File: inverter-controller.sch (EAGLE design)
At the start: 168 parts, among them IC1 STM32F334C8T6, IC10 ISO3082, IC2 SY7152ABC, IC3 LMV358MMX, IC4 LMV358MMX, IC5 SY7152ABC, J1 621006245821, J2 61300211121, J3 CONNECTOR-SMD-2PIN, J4 CONNECTOR-SMD-2PIN, J5 CONNECTOR-SMD-2PIN, X3 0289-9068**15EDGVC-3.81-03P-14, X6 1365-16, Y1 NX2016SA-32M

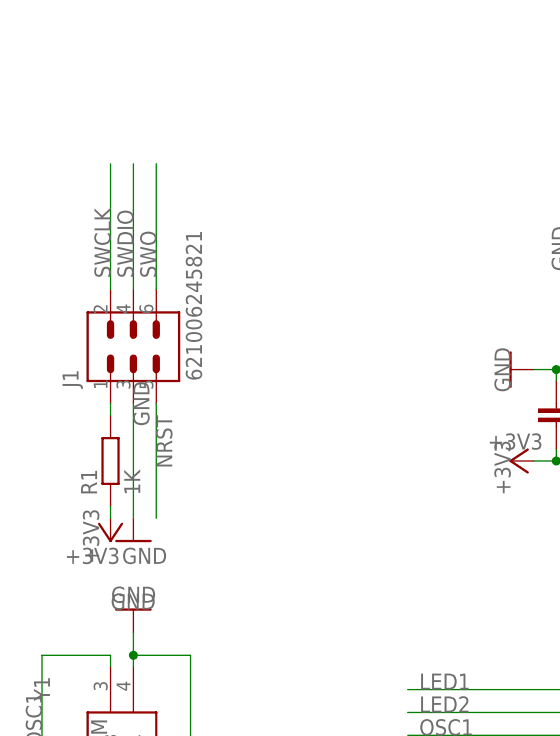
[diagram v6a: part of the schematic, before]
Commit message: Programlama soketi degistirildi.
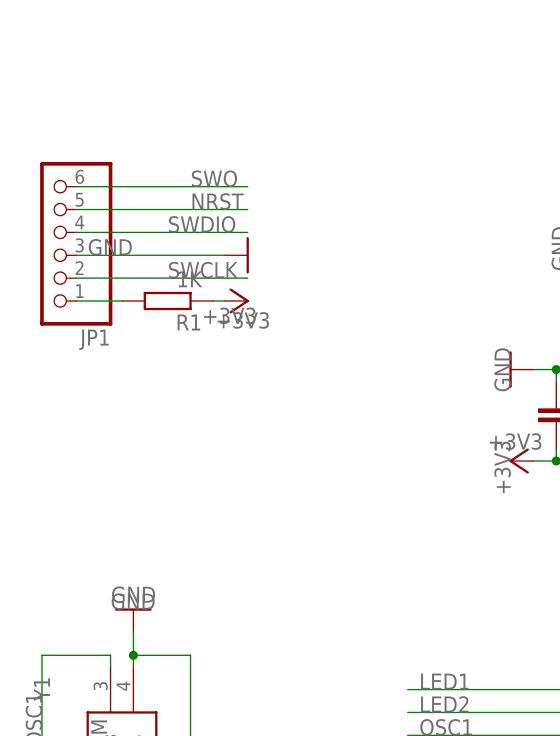
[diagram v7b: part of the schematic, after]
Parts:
- removed J1: 621006245821, Headers:621006245821
- added JP1: (no value), adafruit:PINHD-1X6
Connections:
- removed net N$11: J1.1, R1.2
- new net N$30: JP1.1, R1.2
- net GND: now also JP1.3; no longer J1.3
- net NRST: now also JP1.5; no longer J1.5
- net SWCLK: now also JP1.2; no longer J1.2
- net SWDIO: now also JP1.4; no longer J1.4
- net SWO: now also JP1.6; no longer J1.6
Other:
- moved on the sheet: R1
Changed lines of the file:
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@@
 <part name="TP2" library="testpad" library_urn="urn:adsk.eagle:library:385" deviceset="TP" device="B1,27" package3d_urn="urn:adsk.eagle:package:27944/2"/>
 <part name="TP3" library="testpad" library_urn="urn:adsk.eagle:library:385" deviceset="TP" device="B1,27" package3d_urn="urn:adsk.eagle:package:27944/2"/>
-<part name="J1" library="Headers" library_urn="urn:adsk.eagle:library:11687645" deviceset="621006245821" device="" package3d_urn="urn:adsk.eagle:package:11431832/2"/>
 <part name="+3V1" library="supply1" library_urn="urn:adsk.eagle:library:371" deviceset="+3V3" device=""/>
 <part name="Y1" library="enko" library_urn="urn:adsk.eagle:library:26809666" deviceset="NX2016SA-32M" device="" package3d_urn="urn:adsk.eagle:package:26812247/2"/>
-<part name="GND1" library="supply1" library_urn="urn:adsk.eagle:library:371" deviceset="GND" device=""/>
 <part name="J2" library="Headers" library_urn="urn:adsk.eagle:library:11687645" deviceset="61300211121" device="" package3d_urn="urn:adsk.eagle:package:11390690/2"/>
 <part name="+3V2" library="supply1" library_urn="urn:adsk.eagle:library:371" deviceset="+3V3" device=""/>
@@
 <part name="H3" library="holes" library_urn="urn:adsk.eagle:library:237" deviceset="MOUNT-PAD-ROUND" device="2.8" package3d_urn="urn:adsk.eagle:package:14281/1"/>
 <part name="H4" library="holes" library_urn="urn:adsk.eagle:library:237" deviceset="MOUNT-PAD-ROUND" device="2.8" package3d_urn="urn:adsk.eagle:package:14281/1"/>
+<part name="JP1" library="adafruit" library_urn="urn:adsk.eagle:library:420" deviceset="PINHD-1X6" device="" package3d_urn="urn:adsk.eagle:package:6240711/1"/>
+<part name="GND40" library="supply1" library_urn="urn:adsk.eagle:library:371" deviceset="GND" device=""/>
 </parts>
 <sheets>
@@
 <attribute name="TP_SIGNAL_NAME" x="81.28" y="26.67" size="1.778" layer="97" rot="R180"/>
 </instance>
-<instance part="J1" gate="G$1" x="19.05" y="113.03" smashed="yes" rot="R90">
-<attribute name="NAME" x="12.954" y="109.728" size="1.778" layer="95" rot="R90"/>
-<attribute name="VALUE" x="26.67" y="110.49" size="1.778" layer="96" rot="R90"/>
-</instance>
-<instance part="+3V1" gate="G$1" x="16.51" y="92.71" smashed="yes" rot="R180">
-<attribute name="VALUE" x="15.24" y="90.17" size="1.778" layer="96" rot="R90"/>
+<instance part="+3V1" gate="G$1" x="31.75" y="119.38" smashed="yes" rot="R270">
+<attribute name="VALUE" x="34.29" y="118.11" size="1.778" layer="96" rot="R180"/>
 </instance>
 <instance part="Y1" gate="G$1" x="17.78" y="63.5" smashed="yes" rot="R90">
@@
 <attribute name="VALUE" x="15.24" y="55.88" size="1.778" layer="96" rot="R90" align="center-left"/>
 </instance>
-<instance part="GND1" gate="1" x="19.05" y="92.71" smashed="yes">
-<attribute name="VALUE" x="19.05" y="110.49" size="1.778" layer="96" rot="R270"/>
-</instance>
 <instance part="J2" gate="G$1" x="87.63" y="133.35" smashed="yes" rot="R270">
 <attribute name="NAME" x="91.694" y="135.89" size="1.27" layer="95" rot="R270"/>
@@
 <attribute name="VALUE" x="72.644" y="103.251" size="1.778" layer="96"/>
 </instance>
-<instance part="R1" gate="G$1" x="16.51" y="101.6" smashed="yes" rot="R90">
-<attribute name="NAME" x="15.0114" y="97.79" size="1.778" layer="95" rot="R90"/>
-<attribute name="VALUE" x="19.812" y="97.79" size="1.778" layer="96" rot="R90"/>
+<instance part="R1" gate="G$1" x="22.86" y="119.38" smashed="yes" rot="R180">
+<attribute name="NAME" x="26.67" y="117.8814" size="1.778" layer="95" rot="R180"/>
+<attribute name="VALUE" x="26.67" y="122.682" size="1.778" layer="96" rot="R180"/>
 </instance>
 <instance part="C1" gate="G$1" x="8.89" y="64.77" smashed="yes">
@@
 <attribute name="VALUE" x="61.214" y="-12.6238" size="1.778" layer="96"/>
 </instance>
+<instance part="JP1" gate="A" x="10.16" y="127" smashed="yes" rot="R180">
+<attribute name="NAME" x="16.51" y="116.205" size="1.778" layer="95" rot="R180"/>
+<attribute name="VALUE" x="16.51" y="137.16" size="1.778" layer="96" rot="R180"/>
+</instance>
+<instance part="GND40" gate="1" x="31.75" y="124.46" smashed="yes" rot="R90">
+<attribute name="VALUE" x="13.97" y="124.46" size="1.778" layer="96"/>
+</instance>
 </instances>
 <busses>
@@
 </segment>
 </net>
-<net name="N$11" class="0">
-<segment>
-<pinref part="J1" gate="G$1" pin="1"/>
-<wire x1="16.51" y1="107.95" x2="16.51" y2="106.68" width="0.1524" layer="91"/>
-<pinref part="R1" gate="G$1" pin="2"/>
-</segment>
-</net>
 <net name="+3V3" class="0">
 <segment>
-<wire x1="16.51" y1="96.52" x2="16.51" y2="95.25" width="0.1524" layer="91"/>
-<pinref part="+3V1" gate="G$1" pin="+3V3"/>
-<label x="11.43" y="90.17" size="1.778" layer="95"/>
-<pinref part="R1" gate="G$1" pin="1"/>
-</segment>
-<segment>
 <pinref part="+3V2" gate="G$1" pin="+3V3"/>
 <wire x1="101.6" y1="124.46" x2="99.06" y2="124.46" width="0.1524" layer="91"/>
@@
 <wire x1="378.46" y1="29.21" x2="378.46" y2="22.86" width="0.1524" layer="91"/>
 </segment>
+<segment>
+<pinref part="R1" gate="G$1" pin="1"/>
+<pinref part="+3V1" gate="G$1" pin="+3V3"/>
+<wire x1="27.94" y1="119.38" x2="29.21" y2="119.38" width="0.1524" layer="91"/>
+<label x="26.67" y="116.84" size="1.778" layer="95"/>
+</segment>
 </net>
 <net name="HRTIM1_FLT1" class="0">
@@
 </segment>
 <segment>
-<pinref part="J1" gate="G$1" pin="5"/>
-<wire x1="21.59" y1="107.95" x2="21.59" y2="95.25" width="0.1524" layer="91"/>
-<label x="21.59" y="106.68" size="1.778" layer="95" rot="R270"/>
+<pinref part="JP1" gate="A" pin="5"/>
+<wire x1="12.7" y1="129.54" x2="31.75" y2="129.54" width="0.1524" layer="91"/>
+<label x="25.4" y="129.54" size="1.778" layer="95"/>
 </segment>
 </net>
@@
 <net name="GND" class="0">
 <segment>
-<pinref part="GND1" gate="1" pin="GND"/>
-<pinref part="J1" gate="G$1" pin="3"/>
-<wire x1="19.05" y1="95.25" x2="19.05" y2="107.95" width="0.1524" layer="91"/>
-<label x="17.78" y="90.17" size="1.778" layer="95"/>
-</segment>
-<segment>
 <pinref part="GND3" gate="1" pin="GND"/>
 <wire x1="38.1" y1="43.18" x2="38.1" y2="48.26" width="0.1524" layer="91"/>
@@
 <pinref part="C64" gate="G$1" pin="2"/>
 </segment>
+<segment>
+<pinref part="JP1" gate="A" pin="3"/>
+<wire x1="12.7" y1="124.46" x2="29.21" y2="124.46" width="0.1524" layer="91"/>
+<pinref part="GND40" gate="1" pin="GND"/>
+</segment>
 </net>
 <net name="N$2" class="0">
@@
 </segment>
 <segment>
-<pinref part="J1" gate="G$1" pin="6"/>
-<wire x1="21.59" y1="120.65" x2="21.59" y2="134.62" width="0.1524" layer="91"/>
-<label x="21.59" y="121.92" size="1.778" layer="95" rot="R90"/>
+<pinref part="JP1" gate="A" pin="6"/>
+<wire x1="12.7" y1="132.08" x2="31.75" y2="132.08" width="0.1524" layer="91"/>
+<label x="25.4" y="132.08" size="1.778" layer="95"/>
 </segment>
 </net>
@@
 </segment>
 <segment>
-<pinref part="J1" gate="G$1" pin="4"/>
-<wire x1="19.05" y1="120.65" x2="19.05" y2="134.62" width="0.1524" layer="91"/>
-<label x="19.05" y="121.92" size="1.778" layer="95" rot="R90"/>
+<pinref part="JP1" gate="A" pin="4"/>
+<wire x1="12.7" y1="127" x2="31.75" y2="127" width="0.1524" layer="91"/>
+<label x="22.86" y="127" size="1.778" layer="95"/>
 </segment>
 </net>
@@
 </segment>
 <segment>
-<pinref part="J1" gate="G$1" pin="2"/>
-<wire x1="16.51" y1="120.65" x2="16.51" y2="134.62" width="0.1524" layer="91"/>
-<label x="16.51" y="121.92" size="1.778" layer="95" rot="R90"/>
+<pinref part="JP1" gate="A" pin="2"/>
+<wire x1="12.7" y1="121.92" x2="31.75" y2="121.92" width="0.1524" layer="91"/>
+<label x="22.86" y="121.92" size="1.778" layer="95"/>
 </segment>
 </net>
@@
 </segment>
 </net>
+<net name="N$30" class="0">
+<segment>
+<pinref part="JP1" gate="A" pin="1"/>
+<wire x1="12.7" y1="119.38" x2="17.78" y2="119.38" width="0.1524" layer="91"/>
+<pinref part="R1" gate="G$1" pin="2"/>
+</segment>
+</net>

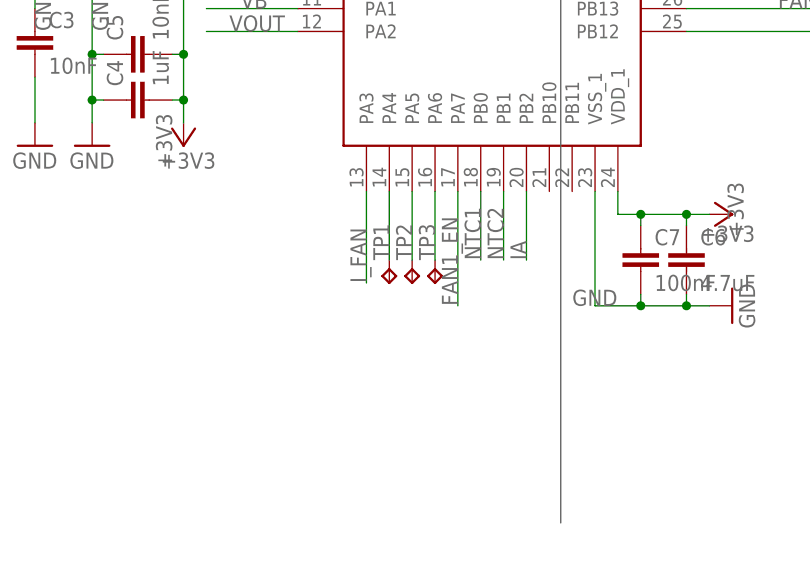
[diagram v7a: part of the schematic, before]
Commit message: DRC Kontrolleri yapıldı Teardrops yapıldı.
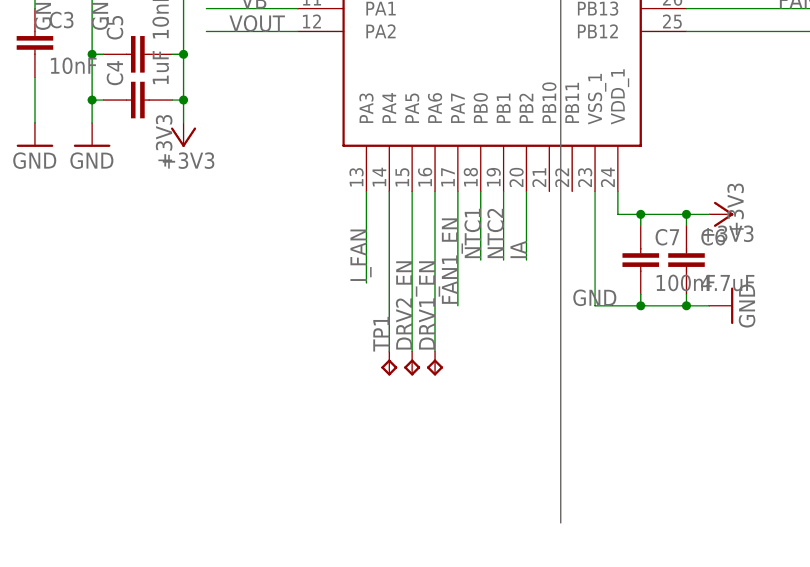
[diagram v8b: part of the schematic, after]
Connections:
- removed net N$4: IC1.PA5, TP2.TP
- removed net N$5: IC1.PA6, TP3.TP
- net DRV1_EN: now also IC1.PA6, TP3.TP
- net DRV2_EN: now also IC1.PA5, TP2.TP
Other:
- moved on the sheet: TP1
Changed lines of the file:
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@@
 <attribute name="VALUE" x="106.68" y="96.52" size="1.778" layer="96" align="center-left"/>
 </instance>
-<instance part="TP1" gate="G$1" x="77.47" y="25.4" smashed="yes" rot="R180">
-<attribute name="NAME" x="77.47" y="27.94" size="1.778" layer="95" rot="R90"/>
-<attribute name="TP_SIGNAL_NAME" x="76.2" y="26.67" size="1.778" layer="97" rot="R180"/>
-</instance>
-<instance part="TP2" gate="G$1" x="80.01" y="25.4" smashed="yes" rot="R180">
-<attribute name="NAME" x="80.01" y="27.94" size="1.778" layer="95" rot="R90"/>
-<attribute name="TP_SIGNAL_NAME" x="78.74" y="26.67" size="1.778" layer="97" rot="R180"/>
-</instance>
-<instance part="TP3" gate="G$1" x="82.55" y="25.4" smashed="yes" rot="R180">
-<attribute name="NAME" x="82.55" y="27.94" size="1.778" layer="95" rot="R90"/>
-<attribute name="TP_SIGNAL_NAME" x="81.28" y="26.67" size="1.778" layer="97" rot="R180"/>
+<instance part="TP1" gate="G$1" x="77.47" y="15.24" smashed="yes" rot="R180">
+<attribute name="NAME" x="77.47" y="17.78" size="1.778" layer="95" rot="R90"/>
+<attribute name="TP_SIGNAL_NAME" x="76.2" y="16.51" size="1.778" layer="97" rot="R180"/>
+</instance>
+<instance part="TP2" gate="G$1" x="80.01" y="15.24" smashed="yes" rot="R180">
+<attribute name="TP_SIGNAL_NAME" x="78.74" y="16.51" size="1.778" layer="97" rot="R180"/>
+</instance>
+<instance part="TP3" gate="G$1" x="82.55" y="15.24" smashed="yes" rot="R180">
+<attribute name="TP_SIGNAL_NAME" x="81.28" y="16.51" size="1.778" layer="97" rot="R180"/>
 </instance>
 <instance part="+3V1" gate="G$1" x="31.75" y="119.38" smashed="yes" rot="R270">
@@
 <segment>
 <pinref part="IC1" gate="G$1" pin="PA4"/>
-<wire x1="77.47" y1="35.56" x2="77.47" y2="27.94" width="0.1524" layer="91"/>
+<wire x1="77.47" y1="35.56" x2="77.47" y2="17.78" width="0.1524" layer="91"/>
 <pinref part="TP1" gate="G$1" pin="TP"/>
-</segment>
-</net>
-<net name="N$4" class="0">
-<segment>
-<pinref part="IC1" gate="G$1" pin="PA5"/>
-<wire x1="80.01" y1="35.56" x2="80.01" y2="27.94" width="0.1524" layer="91"/>
-<pinref part="TP2" gate="G$1" pin="TP"/>
-</segment>
-</net>
-<net name="N$5" class="0">
-<segment>
-<pinref part="IC1" gate="G$1" pin="PA6"/>
-<wire x1="82.55" y1="35.56" x2="82.55" y2="27.94" width="0.1524" layer="91"/>
-<pinref part="TP3" gate="G$1" pin="TP"/>
 </segment>
 </net>
@@
 <pinref part="X6" gate="-10" pin="S"/>
 </segment>
+<segment>
+<pinref part="IC1" gate="G$1" pin="PA6"/>
+<wire x1="82.55" y1="35.56" x2="82.55" y2="17.78" width="0.1524" layer="91"/>
+<pinref part="TP3" gate="G$1" pin="TP"/>
+<label x="82.55" y="17.78" size="1.778" layer="95" rot="R90"/>
+</segment>
 </net>
 <net name="DRV2_EN" class="0">
@@
 <pinref part="X6" gate="-4" pin="S"/>
 </segment>
-</net>
+<segment>
+<pinref part="IC1" gate="G$1" pin="PA5"/>
+<wire x1="80.01" y1="35.56" x2="80.01" y2="17.78" width="0.1524" layer="91"/>
+<pinref part="TP2" gate="G$1" pin="TP"/>
+<label x="80.01" y="17.78" size="1.778" layer="95" rot="R90"/>
+</segment>
+</net>
